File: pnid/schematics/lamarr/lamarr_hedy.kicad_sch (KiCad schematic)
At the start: 103 parts, among them U2 gse_elec_bob_igniter_2:sensor

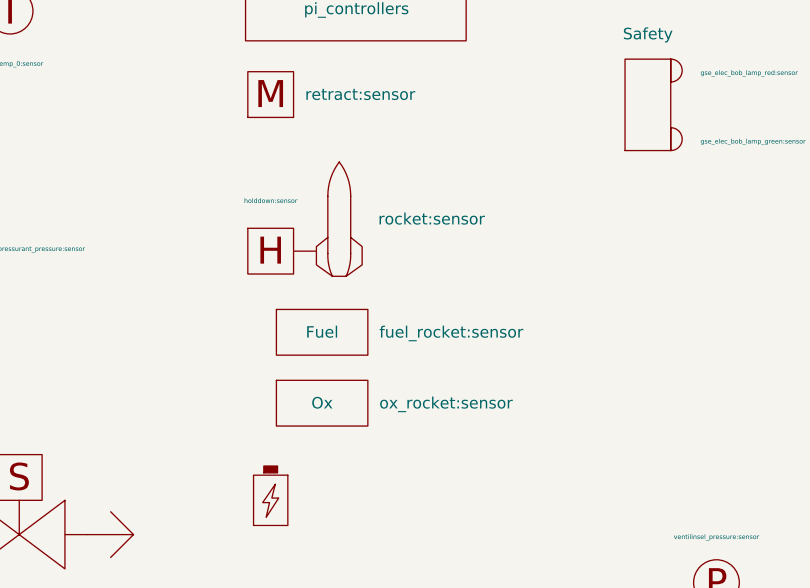
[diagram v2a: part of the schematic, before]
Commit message: remove holddown sensor. we dont use it anymore
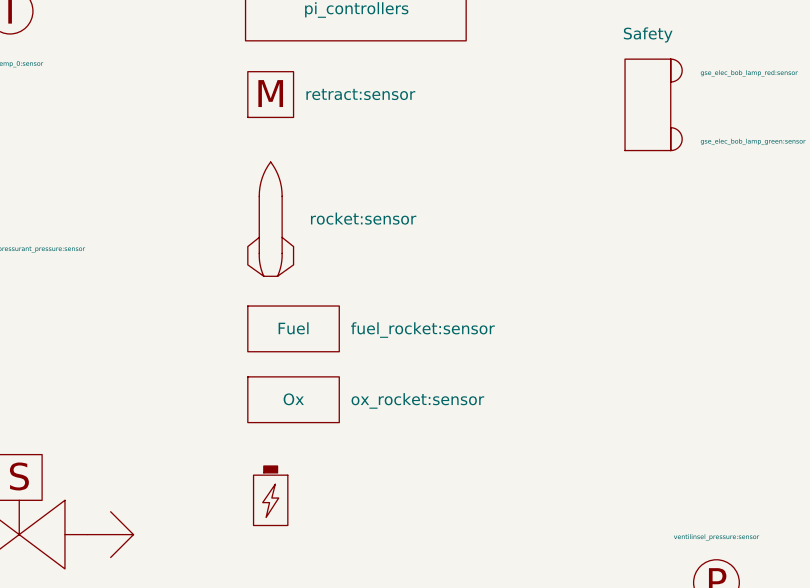
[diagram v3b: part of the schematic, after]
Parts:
- removed Holddown: holddown:sensor, symbol PnID-Lib:heater
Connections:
- net at engine.~ (C): now also venturi1.~; no longer ox_venturi.~
- net at venturi1.~: now also fuel_main_valve.~, fuel_venturi_pressure.~; no longer engine.~ (C)
- net at dewar_needle_valve?.~: now also C2.~, C3.~; no longer C1.~
- new net: engine.~ (C), ox_venturi.~
- new net: OX.~, ox_main_valve.~, ox_quick_connect.~
- new net: DewarOverPressureValve?.~, LOX.~, dewar_pressurize_solenoid.~
- new net: C1.~, dewar_needle_valve?.~
- new net: ox_pressurant_valve.~, ox_pressurant_vent_valve.~, pressurantPressureRegulator2.~
- new net: FUEL.~, fuel_main_valve.~, ox_quick_connect1.~
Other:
- moved on the sheet: Fuel, Ox
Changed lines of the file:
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@@
 	(symbol
 		(lib_id "PnID-Lib:Flowchart_State")
-		(at 169.545 66.675 0)
+		(at 166.37 66.294 0)
 		(unit 1)
 		(exclude_from_sim no)
@@
 		(fields_autoplaced yes)
 		(property "Reference" "Ox"
-			(at 169.545 66.675 0)
+			(at 166.37 66.294 0)
 			(effects
 				(font
@@
 		)
 		(property "Value" "ox_rocket:sensor"
-			(at 175.895 66.6749 0)
+			(at 172.72 66.2939 0)
 			(effects
 				(font
@@
 		)
 		(property "Footprint" ""
-			(at 169.545 66.675 0)
+			(at 166.37 66.294 0)
 			(effects
 				(font
@@
 		)
 		(property "Datasheet" ""
-			(at 169.545 66.675 0)
+			(at 166.37 66.294 0)
 			(effects
 				(font
@@
 		)
 		(property "Description" ""
-			(at 169.545 66.675 0)
+			(at 166.37 66.294 0)
 			(effects
 				(font
@@
 	)
 	(symbol
-		(lib_id "PnID-Lib:heater")
-		(at 163.83 49.784 0)
-		(unit 1)
-		(exclude_from_sim no)
-		(in_bom yes)
-		(on_board yes)
-		(dnp no)
-		(property "Reference" "Holddown"
-			(at 158.75 47.498 0)
-			(effects
-				(font
-					(size 0.508 0.508)
-				)
-				(hide yes)
-			)
-		)
-		(property "Value" "holddown:sensor"
-			(at 163.83 44.196 0)
-			(effects
-				(font
-					(size 0.508 0.508)
-				)
-			)
-		)
-		(property "Footprint" ""
-			(at 163.83 49.784 0)
-			(effects
-				(font
-					(size 1.27 1.27)
-				)
-				(hide yes)
-			)
-		)
-		(property "Datasheet" ""
-			(at 163.83 49.784 0)
-			(effects
-				(font
-					(size 1.27 1.27)
-				)
-				(hide yes)
-			)
-		)
-		(property "Description" "A"
-			(at 163.83 49.784 0)
-			(effects
-				(font
-					(size 1.27 1.27)
-				)
-				(hide yes)
-			)
-		)
-		(pin "~"
-		)
-		(instances
-			(project "lamarr_hedy"
-				(path "/604fc9f3-63a6-4133-afd1-4a5c2507dc1d"
-					(reference "Holddown")
-					(unit 1)
-				)
-			)
-		)
-	)
-	(symbol
 		(lib_name "Valve_Servo_1")
 		(lib_id "PnID-Lib:Valve_Servo")
@@
 	(symbol
 		(lib_id "PnID-Lib:Rocket_Channel")
-		(at 171.45 48.26 0)
+		(at 163.83 48.26 0)
 		(unit 1)
 		(exclude_from_sim no)
@@
 		(dnp no)
 		(property "Reference" "R1"
-			(at 175.514 41.1479 0)
+			(at 167.894 41.1479 0)
 			(effects
 				(font
@@
 		)
 		(property "Value" "rocket:sensor"
-			(at 175.768 46.228 0)
+			(at 168.148 46.228 0)
 			(effects
 				(font
@@
 		)
 		(property "Footprint" ""
-			(at 171.45 51.308 0)
+			(at 163.83 51.308 0)
 			(effects
 				(font
@@
 		)
 		(property "Datasheet" ""
-			(at 171.45 51.308 0)
+			(at 163.83 51.308 0)
 			(effects
 				(font
@@
 		)
 		(property "Description" ""
-			(at 171.45 48.26 0)
+			(at 163.83 48.26 0)
 			(effects
 				(font
@@
 		)
 		(property "Unit" " "
-			(at 175.514 46.2279 0)
+			(at 167.894 46.2279 0)
 			(effects
 				(font
@@
 		)
 		(property "Action_Reference" " "
-			(at 175.514 48.7679 0)
+			(at 167.894 48.7679 0)
 			(effects
 				(font
@@
 		)
 		(property "Data_Content" " "
-			(at 175.514 51.3079 0)
+			(at 167.894 51.3079 0)
 			(effects
 				(font
@@
 	(symbol
 		(lib_id "PnID-Lib:Flowchart_State")
-		(at 169.545 58.801 0)
+		(at 166.37 58.42 0)
 		(unit 1)
 		(exclude_from_sim no)
@@
 		(dnp no)
 		(property "Reference" "Fuel"
-			(at 169.545 58.801 0)
+			(at 166.37 58.42 0)
 			(effects
 				(font
@@
 		)
 		(property "Value" "fuel_rocket:sensor"
-			(at 175.895 58.8009 0)
+			(at 172.72 58.4199 0)
 			(effects
 				(font
@@
 		)
 		(property "Footprint" ""
-			(at 169.545 58.801 0)
+			(at 166.37 58.42 0)
 			(effects
 				(font
@@
 		)
 		(property "Datasheet" ""
-			(at 169.545 58.801 0)
+			(at 166.37 58.42 0)
 			(effects
 				(font
@@
 		)
 		(property "Description" ""
-			(at 169.545 58.801 0)
+			(at 166.37 58.42 0)
 			(effects
 				(font

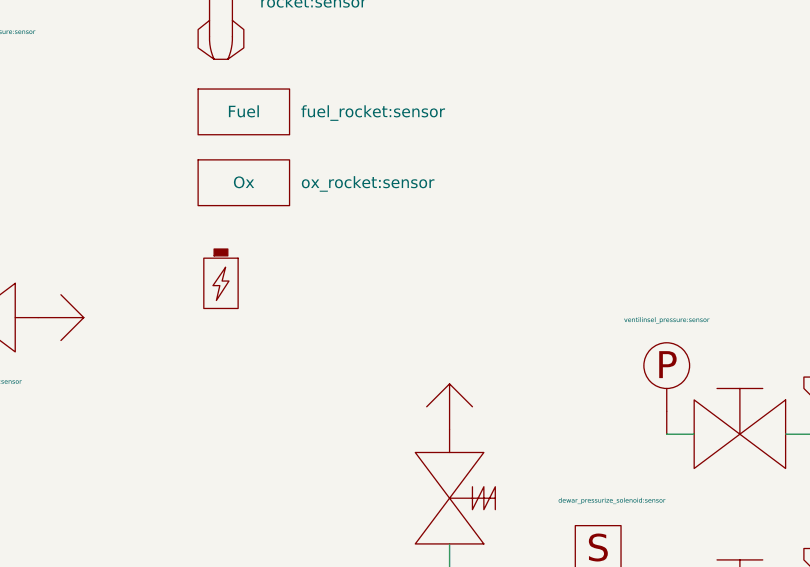
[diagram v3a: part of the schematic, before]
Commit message: improve feedback for battery
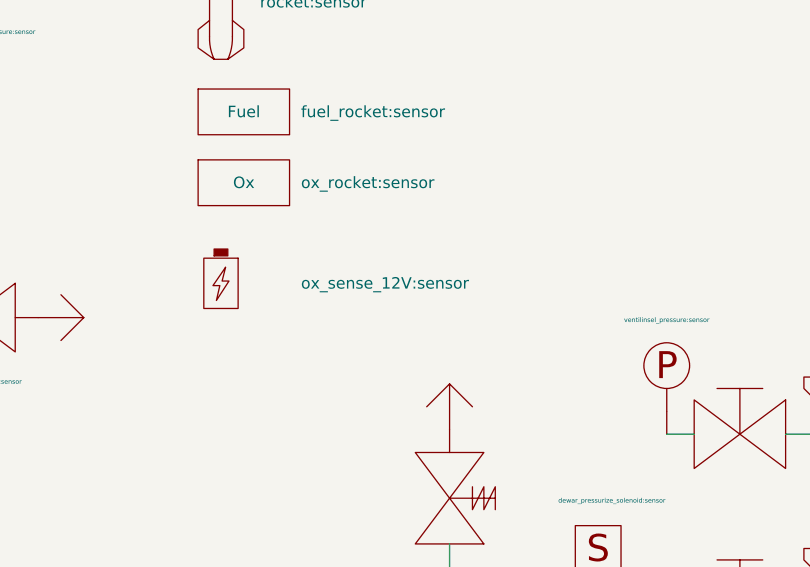
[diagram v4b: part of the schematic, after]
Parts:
- U2: value gse_elec_bob_igniter_2:sensor -> ox_sense_12V:sensor
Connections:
- net at engine.~ (C): now also venturi1.~; no longer ox_venturi.~
- net at venturi1.~: now also fuel_main_valve.~, fuel_venturi_pressure.~; no longer engine.~ (C)
- net at dewar_needle_valve?.~: now also C2.~, C3.~; no longer C1.~
- new net: engine.~ (C), ox_venturi.~
- new net: OX.~, ox_main_valve.~, ox_quick_connect.~
- new net: DewarOverPressureValve?.~, LOX.~, dewar_pressurize_solenoid.~
- new net: C1.~, dewar_needle_valve?.~
- new net: ox_pressurant_valve.~, ox_pressurant_vent_valve.~, pressurantPressureRegulator2.~
- new net: FUEL.~, fuel_main_valve.~, ox_quick_connect1.~
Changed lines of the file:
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@@
 			)
 		)
-		(property "Value" "gse_elec_bob_igniter_2:sensor"
-			(at 163.83 83.82 0)
+		(property "Value" "ox_sense_12V:sensor"
+			(at 172.72 77.47 0)
 			(effects
 				(font
 					(size 1.27 1.27)
 				)
-				(hide yes)
+				(justify left)
 			)
 		)
